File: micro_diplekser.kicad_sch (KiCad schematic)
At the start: 13 parts, among them J1 Antenna [146 MHz|443MHz], J2 146 MHz, J3 443 MHz

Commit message: Last modifications
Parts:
- J2: renamed from J3; value 443 MHz -> 146 MHz
- J3: renamed from J2; value 146 MHz -> 443 MHz
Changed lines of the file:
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@@
 		(dnp no)
 		(fields_autoplaced yes)
-		(property "Reference" "J2"
+		(property "Reference" "J3"
 			(at 107.95 106.9731 0)
 			(effects
@@
 			)
 		)
-		(property "Value" "146 MHz"
+		(property "Value" "443 MHz"
 			(at 107.95 109.5131 0)
 			(effects
@@
 			(project "micro_diplekser"
 				(path "/84a50910-d3ae-4c0b-99ba-a0e6c3a658ed"
-					(reference "J2")
+					(reference "J3")
 					(unit 1)
 				)
@@
 		(on_board yes)
 		(dnp no)
-		(fields_autoplaced yes)
-		(property "Reference" "J3"
+		(property "Reference" "J2"
 			(at 107.95 84.1131 0)
 			(effects
@@
 			)
 		)
-		(property "Value" "443 MHz"
+		(property "Value" "146 MHz"
 			(at 107.95 86.6531 0)
 			(effects
@@
 			(project "micro_diplekser"
 				(path "/84a50910-d3ae-4c0b-99ba-a0e6c3a658ed"
-					(reference "J3")
-					(unit 1)
-				)
+					(reference "J2")
+					(unit 1)
+				)

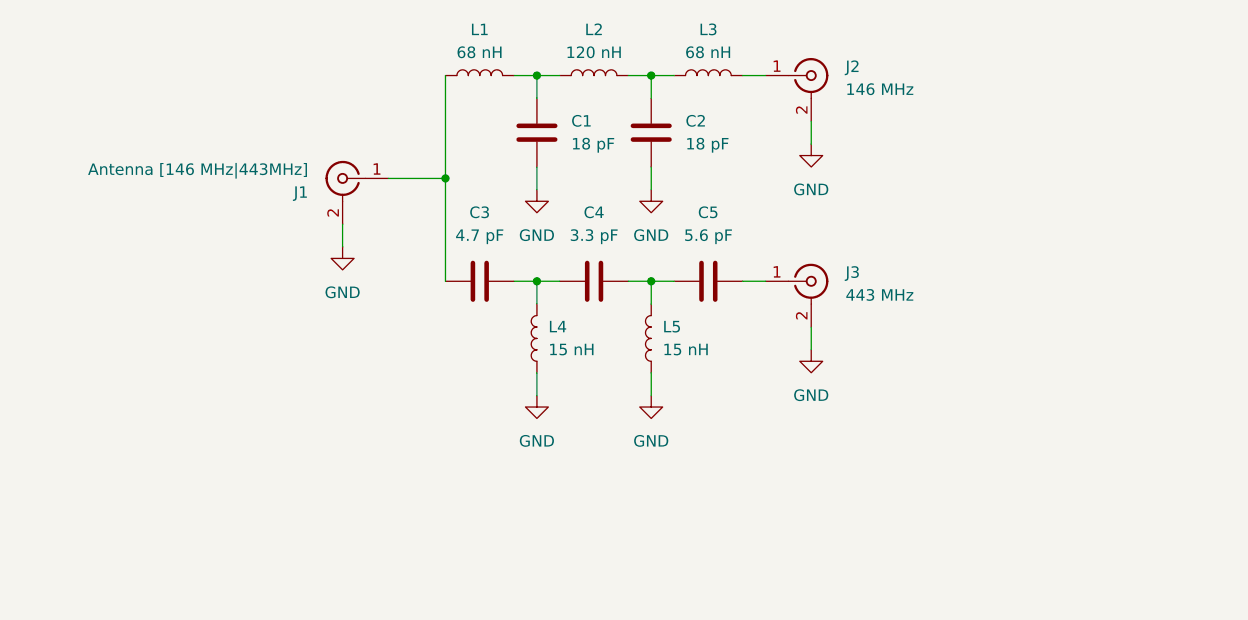
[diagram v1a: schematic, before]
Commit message: Improved version - better S1.1 S2.2 and S3.3 parameters, bigger width and dBm, but decrease isolation between port 3 and port 2 by 5 dBm. Made whole design with 0603 components, not mixing size like in previous design
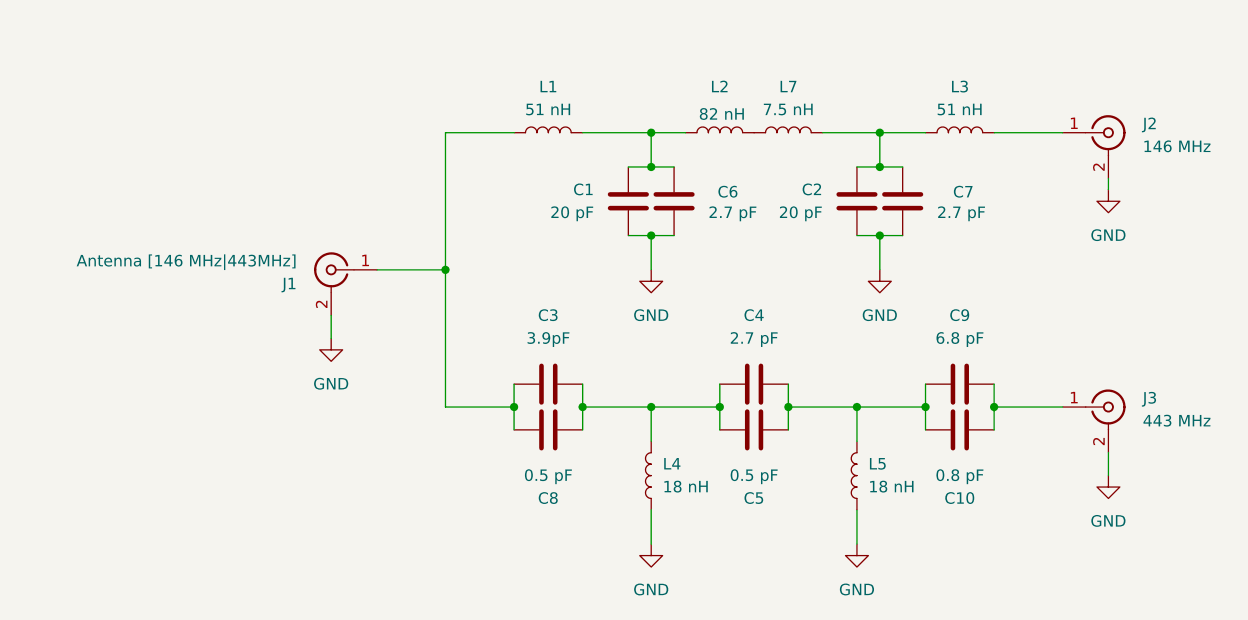
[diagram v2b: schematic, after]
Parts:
- added C10: 0.8 pF, Capacitor_SMD:C_0603_1608Metric, symbol Device:C
- added C6, C7: 2.7 pF, Capacitor_SMD:C_0603_1608Metric, symbol Device:C
- added C8: 0.5 pF, Capacitor_SMD:C_0603_1608Metric, symbol Device:C
- added C9: 6.8 pF, Capacitor_SMD:C_0603_1608Metric, symbol Device:C
- added L7: 7.5 nH, Inductor_SMD:L_0603_1608Metric, symbol Device:L
- C1, C2: value 18 pF -> 20 pF; footprint Capacitor_SMD:C_0402_1005Metric -> Capacitor_SMD:C_0603_1608Metric
- C3: value 4.7 pF -> 3.9pF; footprint Capacitor_SMD:C_0402_1005Metric -> Capacitor_SMD:C_0603_1608Metric
- C4: value 3.3 pF -> 2.7 pF; footprint Capacitor_SMD:C_0402_1005Metric -> Capacitor_SMD:C_0603_1608Metric
- C5: value 5.6 pF -> 0.5 pF; footprint Capacitor_SMD:C_0402_1005Metric -> Capacitor_SMD:C_0603_1608Metric
- L1, L3: value 68 nH -> 51 nH
- L2: value 120 nH -> 82 nH
- L4, L5: value 15 nH -> 18 nH
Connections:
- net GND: now also C6.2, C7.2
- net at C4.2, L5.2: now also C5.2, C10.1, C9.1; no longer C5.1
- net at J3.1 (In): now also C10.2, C9.2; no longer C5.2
- net at C2.1, L3.1: now also C7.1, L7.2; no longer L2.2
- net at C3.2, C4.1, L4.2: now also C5.1, C8.2
- net at C1.1, L1.2, L2.1: now also C6.1
- net at C3.1, J1.1 (In), L1.1: now also C8.1
- new net: L2.2, L7.1
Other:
- moved on the sheet: C1, C3, J1, J2, J3, L1, L3, L4
